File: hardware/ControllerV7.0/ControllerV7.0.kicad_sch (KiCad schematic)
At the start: 9 parts, among them M1 Stepper_Motor_bipolar, M2 Stepper_Motor_bipolar, M3 Stepper_Motor_bipolar, M4 Stepper_Motor_bipolar, M5 Stepper_Motor_bipolar, M6 Stepper_Motor_bipolar

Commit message: Baseline before adding GCode and Planner
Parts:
- added J1: IOBus, symbol Connector_Generic:Conn_02x20_Odd_Even
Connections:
- net +3V3: now also J1.14 (Pin_14), J1.22 (Pin_22), J1.4 (Pin_4)
- net +5V: now also J1.8 (Pin_8)
- net AuxEN: now also J1.24 (Pin_24)
- net Btn1: now also J1.15 (Pin_15)
- net DirJ2: now also J1.23 (Pin_23)
- net GND: now also J1.12 (Pin_12), J1.18 (Pin_18), J1.2 (Pin_2), J1.36 (Pin_36), J1.38 (Pin_38), J1.40 (Pin_40), J1.9 (Pin_9)
- net SCL1: now also J1.1 (Pin_1), J1.11 (Pin_11)
- net SDA1: now also J1.13 (Pin_13), J1.3 (Pin_3)
- net StepJ2: now also J1.21 (Pin_21)
- net TRC0: now also J1.35 (Pin_35)
- net TRC1: now also J1.37 (Pin_37)
- net TRC2: now also J1.39 (Pin_39)
- net U1RX: now also J1.20 (Pin_20)
- net U1TX: now also J1.19 (Pin_19)
- net VDC: now also J1.10 (Pin_10)
- new net 485_A+: J1.6 (Pin_6)
- new net 485_B-: J1.5 (Pin_5)
- new net 485_GND: J1.7 (Pin_7)
- new net Btn2: J1.16 (Pin_16)
- new net Btn3: J1.17 (Pin_17)

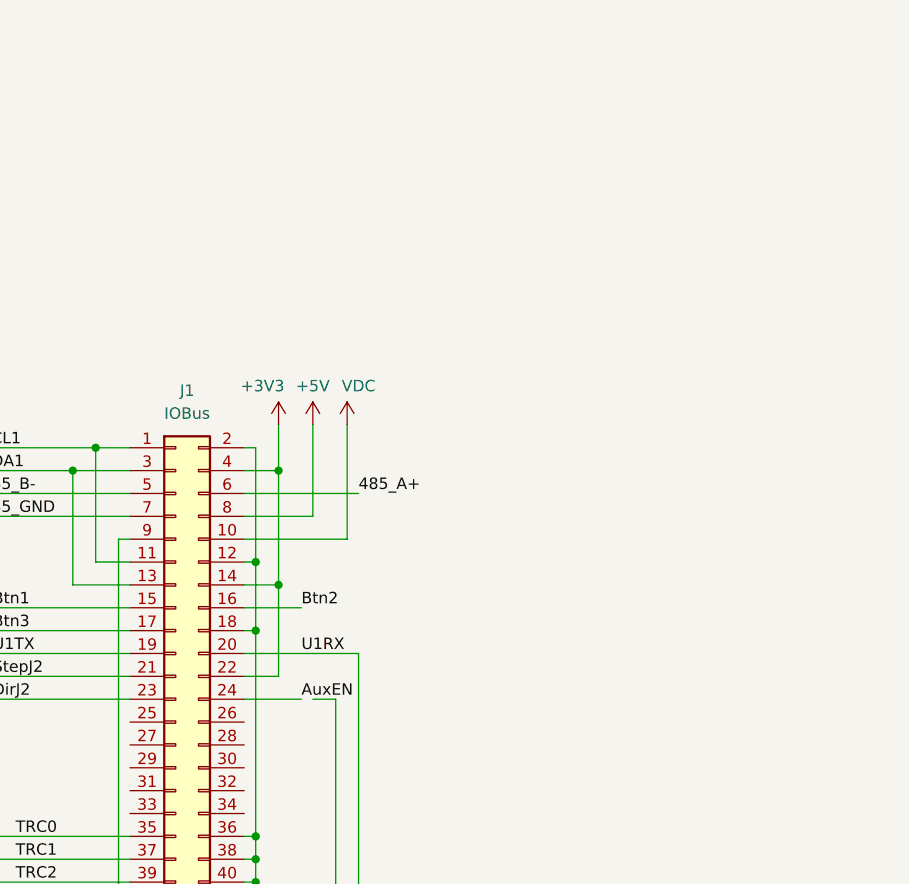
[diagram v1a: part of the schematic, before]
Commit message: base stabile, manca ancora G28 e M400 da sistemare
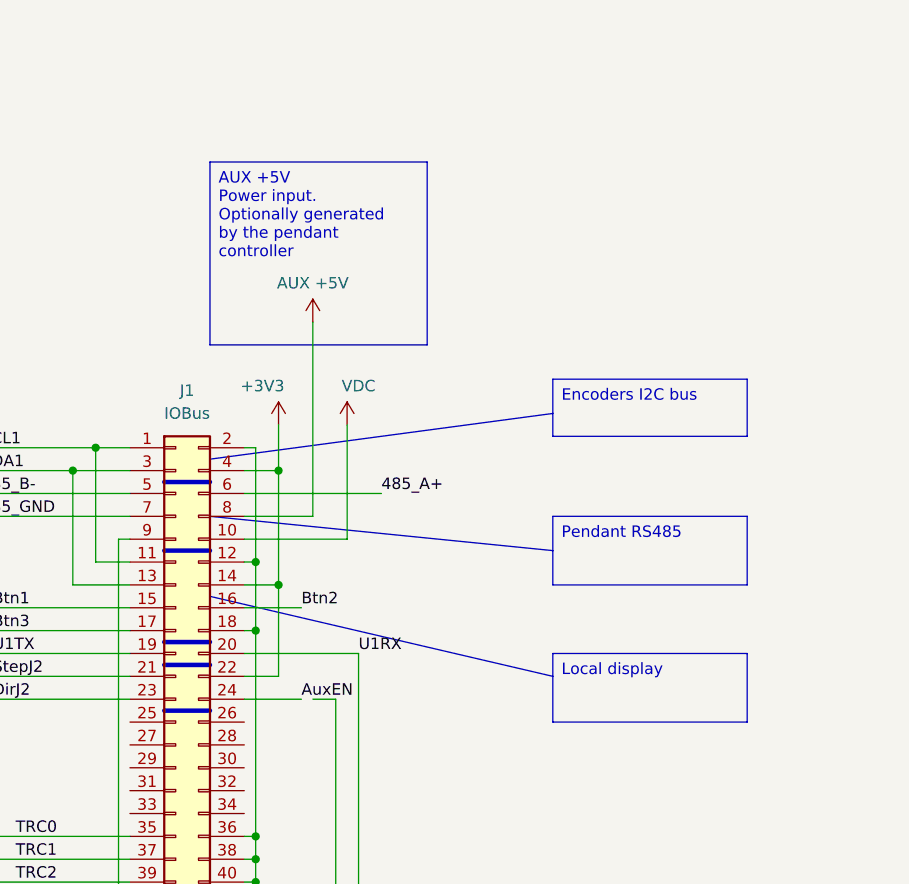
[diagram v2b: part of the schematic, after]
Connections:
- net +5V: no longer J1.8 (Pin_8)
- new net AUX +5V: J1.8 (Pin_8)
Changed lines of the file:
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@@
 		(rev "1.0")
 	)
+	(text_box "Encoders I2C bus\n"
+		(exclude_from_sim no)
+		(at 140.97 172.72 0)
+		(size 21.59 6.35)
+		(margins 0.9525 0.9525 0.9525 0.9525)
+		(stroke
+			(width 0)
+			(type solid)
+			(color 194 0 0 0.5)
+		)
+		(fill
+			(type none)
+		)
+		(effects
+			(font
+				(size 1.27 1.27)
+			)
+			(justify left top)
+		)
+	)
+	(text_box "Pendant RS485\n"
+		(exclude_from_sim no)
+		(at 140.97 187.96 0)
+		(size 21.59 7.62)
+		(margins 0.9525 0.9525 0.9525 0.9525)
+		(stroke
+			(width 0)
+			(type solid)
+			(color 194 0 0 0.49)
+		)
+		(fill
+			(type none)
+		)
+		(effects
+			(font
+				(size 1.27 1.27)
+			)
+			(justify left top)
+		)
+	)
+	(text_box "Local display\n"
+		(exclude_from_sim no)
+		(at 140.97 203.2 0)
+		(size 21.59 7.62)
+		(margins 0.9525 0.9525 0.9525 0.9525)
+		(stroke
+			(width 0)
+			(type solid)
+			(color 194 0 0 0.5)
+		)
+		(fill
+			(type none)
+		)
+		(effects
+			(font
+				(size 1.27 1.27)
+			)
+			(justify left top)
+		)
+	)
+	(text_box "AUX +5V\nPower input. Optionally generated by the pendant controller"
+		(exclude_from_sim no)
+		(at 102.87 148.59 0)
+		(size 24.13 20.32)
+		(margins 0.9525 0.9525 0.9525 0.9525)
+		(stroke
+			(width 0)
+			(type solid)
+		)
+		(fill
+			(type none)
+		)
+		(effects
+			(font
+				(size 1.27 1.27)
+			)
+			(justify left top)
+		)
+	)
 	(junction
 		(at 87.63 182.88)
@@
 		)
 	)
+	(polyline
+		(pts
+			(xy 102.87 187.96) (xy 140.97 191.77)
+		)
+		(stroke
+			(width 0)
+			(type solid)
+			(color 194 0 0 0.5)
+		)
+	)
 	(wire
 		(pts
@@
 		)
 	)
+	(polyline
+		(pts
+			(xy 97.79 209.55) (xy 102.87 209.55)
+		)
+		(stroke
+			(width 0.5)
+			(type solid)
+		)
+	)
 	(wire
 		(pts
@@
 	(wire
 		(pts
-			(xy 106.68 185.42) (xy 119.38 185.42)
+			(xy 106.68 185.42) (xy 121.92 185.42)
 		)
 		(stroke
@@
 		)
 	)
+	(polyline
+		(pts
+			(xy 102.87 181.61) (xy 140.97 176.53)
+		)
+		(stroke
+			(width 0)
+			(type solid)
+			(color 194 0 0 0.5)
+		)
+	)
 	(wire
 		(pts
@@
 		)
 	)
+	(polyline
+		(pts
+			(xy 102.87 196.85) (xy 140.97 205.74)
+		)
+		(stroke
+			(width 0)
+			(type solid)
+			(color 255 0 0 0.5)
+		)
+	)
 	(wire
 		(pts
@@
 		)
 	)
+	(polyline
+		(pts
+			(xy 97.79 201.93) (xy 102.87 201.93)
+		)
+		(stroke
+			(width 0.5)
+			(type solid)
+		)
+	)
 	(wire
 		(pts
@@
 		)
 	)
+	(polyline
+		(pts
+			(xy 97.79 191.77) (xy 102.87 191.77)
+		)
+		(stroke
+			(width 0.5)
+			(type solid)
+		)
+	)
 	(bus
 		(pts
@@
 		)
 	)
+	(polyline
+		(pts
+			(xy 97.79 204.47) (xy 102.87 204.47)
+		)
+		(stroke
+			(width 0.5)
+			(type solid)
+		)
+	)
 	(wire
 		(pts
@@
 		)
 	)
+	(polyline
+		(pts
+			(xy 97.79 184.15) (xy 102.87 184.15)
+		)
+		(stroke
+			(width 0.5)
+			(type solid)
+		)
+	)
 	(wire
 		(pts
@@
 	(wire
 		(pts
-			(xy 114.3 177.8) (xy 114.3 187.96)
+			(xy 114.3 166.37) (xy 114.3 187.96)
 		)
 		(stroke
@@
 	)
 	(label "485_A+"
-		(at 119.38 185.42 0)
+		(at 121.92 185.42 0)
 		(effects
 			(font
@@
 	)
 	(label "U1RX"
-		(at 113.03 203.2 0)
+		(at 119.38 203.2 0)
 		(effects
 			(font
@@
 	(symbol
 		(lib_id "power:+5V")
-		(at 114.3 177.8 0)
+		(at 114.3 166.37 0)
 		(unit 1)
 		(exclude_from_sim no)
@@
 		(dnp no)
 		(property "Reference" "#PWR012"
-			(at 114.3 181.61 0)
+			(at 114.3 170.18 0)
 			(effects
 				(font
@@
 			)
 		)
-		(property "Value" "+5V"
-			(at 114.3 173.482 0)
+		(property "Value" "AUX +5V"
+			(at 114.3 162.052 0)
 			(effects
 				(font
@@
 		)
 		(property "Footprint" ""
-			(at 114.3 177.8 0)
+			(at 114.3 166.37 0)
 			(effects
 				(font
@@
 		)
 		(property "Datasheet" ""
-			(at 114.3 177.8 0)
+			(at 114.3 166.37 0)
 			(effects
 				(font
@@
 		)
 		(property "Description" "Power symbol creates a global label with name \"+5V\""
-			(at 114.3 177.8 0)
+			(at 114.3 166.37 0)
 			(effects
 				(font
